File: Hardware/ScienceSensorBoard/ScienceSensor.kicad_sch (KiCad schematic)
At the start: 93 parts, among them J1 Conn_02x03_Counter_Clockwise, J2 RJ45_LED_Shielded, Q1 SI4156DY, Q10 BSS138, Q11 SI4156DY, Q2 SI4156DY, Q3 SI4156DY, Q4 BSS138, Q5 BSS138, Q6 BSS138, Q7 BSS138, Q8 BSS138, Q9 BSS138, U1 TSR_1-2450, U2 OKI-78SR-3.3_1.5-W36H-C, U3 Teensy4.1_DEV-16771, U6 IRS2005S, U7 IRS2005S

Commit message: Labels
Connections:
- net +12V: now also Conn6.1; no longer Conn6.2
- net GND: now also Conn6.2; no longer Conn6.3
- net Micro_ENC: now also Conn6.3; no longer Conn6.1
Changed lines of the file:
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@@
     (stroke (width 0) (type default) (color 0 0 0 0))
   )
-  (wire (pts (xy 123.825 72.39) (xy 123.825 78.105))
+  (wire (pts (xy 130.175 64.77) (xy 124.46 64.77))
     (stroke (width 0) (type default) (color 0 0 0 0))
   )
@@
     (stroke (width 0) (type default) (color 0 0 0 0))
   )
-  (wire (pts (xy 132.715 72.39) (xy 133.985 72.39))
+  (wire (pts (xy 127.635 71.12) (xy 127.635 73.025))
     (stroke (width 0) (type default) (color 0 0 0 0))
   )
@@
     (stroke (width 0) (type default) (color 0 0 0 0))
   )
-  (wire (pts (xy 127.635 72.39) (xy 127.635 73.025))
+  (wire (pts (xy 124.46 64.77) (xy 124.46 65.405))
     (stroke (width 0) (type default) (color 0 0 0 0))
   )
@@
     (stroke (width 0) (type default) (color 0 0 0 0))
   )
-  (wire (pts (xy 123.825 72.39) (xy 127.635 72.39))
+  (wire (pts (xy 130.175 64.77) (xy 130.175 73.025))
     (stroke (width 0) (type default) (color 0 0 0 0))
   )
@@
     (stroke (width 0) (type default) (color 0 0 0 0))
   )
-  (wire (pts (xy 130.175 71.12) (xy 130.175 73.025))
-    (stroke (width 0) (type default) (color 0 0 0 0))
-  )
   (wire (pts (xy 180.34 109.22) (xy 180.34 110.49))
     (stroke (width 0) (type default) (color 0 0 0 0))
@@
   )
   (wire (pts (xy 162.56 101.6) (xy 162.56 95.25))
+    (stroke (width 0) (type default) (color 0 0 0 0))
+  )
+  (wire (pts (xy 126.365 71.12) (xy 127.635 71.12))
     (stroke (width 0) (type default) (color 0 0 0 0))
   )
@@
     )
   )
-  (global_label "Micro_ENC" (shape output) (at 133.985 72.39 0) (fields_autoplaced)
-    (effects (font (size 1.27 1.27)) (justify left))
-    (property "Intersheet References" "${INTERSHEET_REFS}" (id 0) (at 146.1063 72.3106 0)
-      (effects (font (size 1.27 1.27)) (justify left) hide)
+  (global_label "Micro_ENC" (shape output) (at 126.365 71.12 180) (fields_autoplaced)
+    (effects (font (size 1.27 1.27)) (justify right))
+    (property "Intersheet References" "${INTERSHEET_REFS}" (id 0) (at 114.2437 71.1994 0)
+      (effects (font (size 1.27 1.27)) (justify right) hide)
     )
   )
@@
     (pin "2")
   )
-  (symbol (lib_id "power:+12V") (at 130.175 71.12 0) (unit 1)
-    (in_bom yes) (on_board yes) (fields_autoplaced)
-    (property "Reference" "#PWR0101" (id 0) (at 130.175 74.93 0)
-      (effects (font (size 1.27 1.27)) hide)
-    )
-    (property "Value" "+12V" (id 1) (at 130.175 67.5442 0))
-    (property "Footprint" "" (id 2) (at 130.175 71.12 0)
-      (effects (font (size 1.27 1.27)) hide)
-    )
-    (property "Datasheet" "" (id 3) (at 130.175 71.12 0)
+  (symbol (lib_id "power:+12V") (at 132.715 72.39 0) (unit 1)
+    (in_bom yes) (on_board yes) (fields_autoplaced)
+    (property "Reference" "#PWR0101" (id 0) (at 132.715 76.2 0)
+      (effects (font (size 1.27 1.27)) hide)
+    )
+    (property "Value" "+12V" (id 1) (at 132.715 68.8142 0))
+    (property "Footprint" "" (id 2) (at 132.715 72.39 0)
+      (effects (font (size 1.27 1.27)) hide)
+    )
+    (property "Datasheet" "" (id 3) (at 132.715 72.39 0)
       (effects (font (size 1.27 1.27)) hide)
     )
@@
     (pin "3")
   )
-  (symbol (lib_id "power:GND") (at 123.825 78.105 0) (unit 1)
-    (in_bom yes) (on_board yes)
-    (property "Reference" "#PWR014" (id 0) (at 123.825 84.455 0)
-      (effects (font (size 1.27 1.27)) hide)
-    )
-    (property "Value" "GND" (id 1) (at 120.65 80.01 0))
-    (property "Footprint" "" (id 2) (at 123.825 78.105 0)
-      (effects (font (size 1.27 1.27)) hide)
-    )
-    (property "Datasheet" "" (id 3) (at 123.825 78.105 0)
-      (effects (font (size 1.27 1.27)) hide)
-    )
+  (symbol (lib_id "power:GND") (at 124.46 65.405 0) (unit 1)
+    (in_bom yes) (on_board yes)
+    (property "Reference" "#PWR014" (id 0) (at 124.46 71.755 0)
+      (effects (font (size 1.27 1.27)) hide)
+    )
+    (property "Value" "GND" (id 1) (at 121.285 67.31 0))
+    (property "Footprint" "" (id 2) (at 124.46 65.405 0)
+      (effects (font (size 1.27 1.27)) hide)
+    )
+    (property "Datasheet" "" (id 3) (at 124.46 65.405 0)
+      (effects (font (size 1.27 1.27)) hide)
+    )

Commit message: Molex_SL_06
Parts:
- removed Conn4: Molex_SL_07, MRDT_Connectors:MOLEX_SL_07_Horizontal, symbol MRDT_Connectors:Molex_SL_07
- added Conn4: Molex_SL_06, UVLEDs:705550040, symbol Molex_SL_06:Molex_SL_06
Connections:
- net +12V: now also Conn4.1
- net GND: now also Conn4.2
- net LED_275: now also Conn4.4
- net LED_280: now also Conn4.5
- net LED_315: now also Conn4.6
- no-connect marks 39 -> 38
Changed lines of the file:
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@@
   (no_connect (at 78.105 267.97))
   (no_connect (at 37.465 227.33))
-  (no_connect (at 297.18 24.765))
   (no_connect (at 37.465 234.95))
   (no_connect (at 78.105 199.39))
@@
     (stroke (width 0) (type default) (color 0 0 0 0))
   )
-  (wire (pts (xy 292.1 34.925) (xy 292.1 38.1))
+  (wire (pts (xy 292.1 32.385) (xy 292.1 38.1))
     (stroke (width 0) (type default) (color 0 0 0 0))
   )
@@
     (stroke (width 0) (type default) (color 0 0 0 0))
   )
-  (wire (pts (xy 297.18 34.925) (xy 292.1 34.925))
+  (wire (pts (xy 297.18 32.385) (xy 292.1 32.385))
     (stroke (width 0) (type default) (color 0 0 0 0))
   )
@@
     (stroke (width 0) (type default) (color 0 0 0 0))
   )
-  (wire (pts (xy 281.305 35.56) (xy 281.305 32.385))
+  (wire (pts (xy 281.305 29.845) (xy 281.305 35.56))
     (stroke (width 0) (type default) (color 0 0 0 0))
   )
@@
     (stroke (width 0) (type default) (color 0 0 0 0))
   )
-  (wire (pts (xy 259.715 27.305) (xy 297.18 27.305))
+  (wire (pts (xy 259.715 24.765) (xy 297.18 24.765))
     (stroke (width 0) (type default) (color 0 0 0 0))
   )
@@
     (stroke (width 0) (type default) (color 0 0 0 0))
   )
-  (wire (pts (xy 270.51 33.02) (xy 270.51 29.845))
+  (wire (pts (xy 270.51 27.305) (xy 270.51 33.02))
     (stroke (width 0) (type default) (color 0 0 0 0))
   )
@@
     (stroke (width 0) (type default) (color 0 0 0 0))
   )
-  (wire (pts (xy 270.51 29.845) (xy 297.18 29.845))
+  (wire (pts (xy 270.51 27.305) (xy 297.18 27.305))
     (stroke (width 0) (type default) (color 0 0 0 0))
   )
@@
     (stroke (width 0) (type default) (color 0 0 0 0))
   )
-  (wire (pts (xy 281.305 32.385) (xy 297.18 32.385))
+  (wire (pts (xy 281.305 29.845) (xy 297.18 29.845))
     (stroke (width 0) (type default) (color 0 0 0 0))
   )
@@
     (pin "3")
   )
-  (symbol (lib_id "MRDT_Connectors:Molex_SL_07") (at 302.26 36.195 0) (unit 1)
-    (in_bom yes) (on_board yes)
-    (property "Reference" "Conn4" (id 0) (at 301.625 38.2816 0)
-      (effects (font (size 1.524 1.524)) (justify left))
-    )
-    (property "Value" "Molex_SL_07" (id 1) (at 301.625 41.275 0)
-      (effects (font (size 1.524 1.524)) (justify left))
-    )
-    (property "Footprint" "MRDT_Connectors:MOLEX_SL_07_Horizontal" (id 2) (at 302.26 31.115 0)
-      (effects (font (size 1.524 1.524)) hide)
-    )
-    (property "Datasheet" "" (id 3) (at 302.26 31.115 0)
-      (effects (font (size 1.524 1.524)) hide)
-    )
-    (pin "1")
-    (pin "2")
-    (pin "3")
-    (pin "4")
-    (pin "5")
-    (pin "6")
-    (pin "7")
-  )
   (symbol (lib_id "power:+5V") (at 137.16 20.32 0) (unit 1)
     (in_bom yes) (on_board yes) (fields_autoplaced)
@@
     (pin "1")
   )
+  (symbol (lib_id "Molex_SL_06:Molex_SL_06") (at 302.26 31.115 0) (unit 1)
+    (in_bom yes) (on_board yes) (fields_autoplaced)
+    (property "Reference" "Conn4" (id 0) (at 305.435 25.0588 0)
+      (effects (font (size 1.524 1.524)) (justify left))
+    )
+    (property "Value" "Molex_SL_06" (id 1) (at 305.435 28.0522 0)
+      (effects (font (size 1.524 1.524)) (justify left))
+    )
+    (property "Footprint" "UVLEDs:705550040" (id 2) (at 302.26 31.115 0)
+      (effects (font (size 1.524 1.524)) hide)
+    )
+    (property "Datasheet" "" (id 3) (at 302.26 31.115 0)
+      (effects (font (size 1.524 1.524)) hide)
+    )
+    (pin "1")
+    (pin "2")
+    (pin "3")
+    (pin "4")
+    (pin "5")
+    (pin "6")
+  )
   (symbol (lib_id "power:GND") (at 294.005 57.15 90) (unit 1)
     (in_bom yes) (on_board yes)
@@
       (reference "Conn3") (unit 1) (value "Molex_SL_02") (footprint "MRDT_Connectors:MOLEX_SL_02_Horizontal")
     )
-    (path "/2cca1221-a56d-46b9-abdb-f313a2558695"
-      (reference "Conn4") (unit 1) (value "Molex_SL_07") (footprint "MRDT_Connectors:MOLEX_SL_07_Horizontal")
+    (path "/e8ba4c58-43c8-4e60-828b-fab781a9437e"
+      (reference "Conn4") (unit 1) (value "Molex_SL_06") (footprint "UVLEDs:705550040")
     )
     (path "/726f2370-5511-4905-9eb4-028092273805"

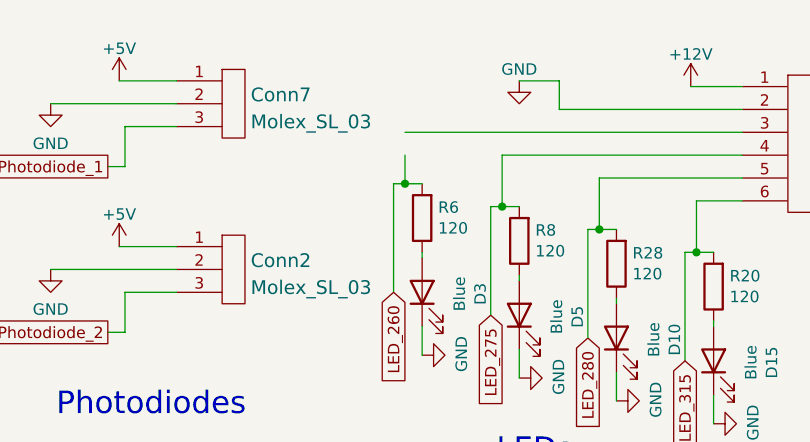
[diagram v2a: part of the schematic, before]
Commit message: Fixed Schematic error, Labeled some LEDs
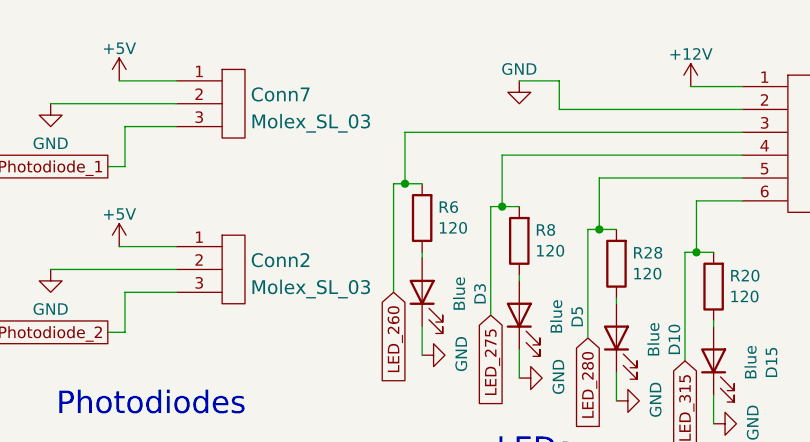
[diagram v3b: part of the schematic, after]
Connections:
- net LED_260: now also Conn4.3
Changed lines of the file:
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@@
-    (stroke (width 0) (type default) (color 0 0 0 0))
-  )
-  (wire (pts (xy 259.715 30.48) (xy 259.715 27.305))
     (stroke (width 0) (type default) (color 0 0 0 0))
   )
@@
     (stroke (width 0) (type default) (color 0 0 0 0))
   )
+  (wire (pts (xy 259.715 24.765) (xy 259.715 30.48))
+    (stroke (width 0) (type default) (color 0 0 0 0))
+  )

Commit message: Replaced HBridge & Encoder w/ servo
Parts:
- removed C10, C8: 0.1u, Capacitor_SMD:C_0603_1608Metric_Pad1.08x0.95mm_HandSolder, symbol Device:C
- removed C9: 10u, Capacitor_SMD:C_0603_1608Metric_Pad1.08x0.95mm_HandSolder, symbol Device:C_Small
- removed Conn5: AndersonPP, MRDT_Connectors:Square_Anderson_2_H_Side_By_Side, symbol MRDT_Connectors:AndersonPP
- removed Conn6: Molex_SL_03, MRDT_Connectors:MOLEX_SL_03_Horizontal, symbol MRDT_Connectors:Molex_SL_03
- removed D11, D14: D_Small, Diode_SMD:D_0603_1608Metric_Pad1.05x0.95mm_HandSolder, symbol Device:D_Small
- removed D12, D13: Pink, LED_SMD:LED_0603_1608Metric_Pad1.05x0.95mm_HandSolder, symbol Device:LED_Small
- removed Q1, Q11, Q2, Q3: SI4156DY, Package_SO:SOIC-8_3.9x4.9mm_P1.27mm, symbol Transistor_FET:FDS2734
- removed R29, R30, R33, R34: 100, Resistor_SMD:R_0603_1608Metric_Pad0.98x0.95mm_HandSolder, symbol Device:R
- removed R31, R32: 120, Resistor_SMD:R_0603_1608Metric_Pad0.98x0.95mm_HandSolder, symbol Device:R
- removed U6, U7: IRS2005S, Package_SO:SOIC-8_3.9x4.9mm_P1.27mm, symbol Driver_FET:IRS2005S
- added Conn?: Molex_SL_03, MRDT_Connectors:MOLEX_SL_03_Horizontal, symbol MRDT_Connectors:Molex_SL_03
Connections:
- net +5V: now also Conn?.1
- net GND: now also Conn?.2
- net Micro_Servo2: now reaches U3.38 (A14)
- net Micro_Servo2: now also Conn?.3
- net Micro_ENC: no longer names the net of U3.21 (A7)
- net Micro_FWD: no longer names the net of U3.14 (A0)
- net Micro_RVS: no longer names the net of U3.15 (A1)
- net Micro_Servo renamed Micro_Servo1
- no-connect marks 38 -> 40
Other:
- note added: "To be updated with new detector"
- note removed: "Encoder"
- note removed: "H-Bridge"
- moved on the sheet: Conn2, Conn3, Conn4, Conn7, D10, D15, D3, D4, D5, R20, R28, R6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

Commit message: CCD, LED changes
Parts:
- removed Conn2, Conn7: Molex_SL_03, MRDT_Connectors:MOLEX_SL_03_Horizontal, symbol MRDT_Connectors:Molex_SL_03
- added Conn?: Molex_SL_06, UVLEDs:705550040, symbol Molex_SL_06:Molex_SL_06
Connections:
- net +3V3: now also Conn?.1
- net GND: now also Conn?.2
- net CCD_ICG: now reaches U3.39 (A15)
- net CCD_ICG: now also Conn?.5
- net CCD_SH: now reaches U3.40 (A16)
- net CCD_SH: now also Conn?.4
- net Photodiode_1 renamed CCD_MC
- net CCD_MC: now also Conn?.3
- net Photodiode_2 renamed CCD_OS
- net CCD_OS: now also Conn?.6
- no-connect marks 40 -> 37
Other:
- note added: "LEDs & Detector"
- note added: "TCD1304AP CCD"
- note removed: "LEDs & Photodiode"
- note removed: "Photodiodes"
- note removed: "To be updated with new detector"

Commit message: Layout updated for LEDs and Science Sensor Board, schematic for CCD
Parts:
- gave numbers to parts that had none: 2
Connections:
- net Micro_Servo2: now also U3.23 (A9); no longer U3.38 (A14)
- no-connect marks 37 -> 38
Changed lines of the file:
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@@
   )
   (no_connect (at 37.465 240.03))
+  (no_connect (at 78.105 255.27))
   (no_connect (at 78.105 229.87))
   (no_connect (at 94.615 168.91))
@@
     (stroke (width 0) (type default) (color 0 0 0 0))
   )
-  (wire (pts (xy 78.105 255.27) (xy 83.185 255.27))
+  (wire (pts (xy 78.105 267.97) (xy 83.185 267.97))
     (stroke (width 0) (type default) (color 0 0 0 0))
   )
@@
     )
   )
-  (global_label "Micro_Servo2" (shape output) (at 83.185 255.27 0) (fields_autoplaced)
+  (global_label "Micro_Servo2" (shape output) (at 83.185 267.97 0) (fields_autoplaced)
     (effects (font (size 1 1)) (justify left))
-    (property "Intersheet References" "${INTERSHEET_REFS}" (id 0) (at 94.8245 255.2075 0)
+    (property "Intersheet References" "${INTERSHEET_REFS}" (id 0) (at 94.8245 267.9075 0)
       (effects (font (size 1 1)) (justify left) hide)
     )
@@
   (symbol (lib_id "MRDT_Connectors:Molex_SL_03") (at 147.955 47.625 0) (unit 1)
     (in_bom yes) (on_board yes) (fields_autoplaced)
-    (property "Reference" "Conn?" (id 0) (at 151.13 42.8388 0)
+    (property "Reference" "Conn2" (id 0) (at 151.13 42.8388 0)
       (effects (font (size 1.524 1.524)) (justify left))
     )
@@
   (symbol (lib_id "Molex_SL_06:Molex_SL_06") (at 271.78 99.695 0) (unit 1)
     (in_bom yes) (on_board yes) (fields_autoplaced)
-    (property "Reference" "Conn?" (id 0) (at 274.955 93.6388 0)
+    (property "Reference" "Conn5" (id 0) (at 274.955 93.6388 0)
       (effects (font (size 1.524 1.524)) (justify left))
     )
@@
   (symbol (lib_id "power:+3V3") (at 260.35 88.265 0) (unit 1)
     (in_bom yes) (on_board yes) (fields_autoplaced)
-    (property "Reference" "#PWR?" (id 0) (at 260.35 92.075 0)
+    (property "Reference" "#PWR037" (id 0) (at 260.35 92.075 0)
       (effects (font (size 1.27 1.27)) hide)
     )
@@
   (symbol (lib_id "power:+5V") (at 136.525 41.275 0) (unit 1)
     (in_bom yes) (on_board yes) (fields_autoplaced)
-    (property "Reference" "#PWR?" (id 0) (at 136.525 45.085 0)
+    (property "Reference" "#PWR022" (id 0) (at 136.525 45.085 0)
       (effects (font (size 1.27 1.27)) hide)
     )
@@
   (symbol (lib_id "power:GND") (at 125.095 43.815 0) (unit 1)
     (in_bom yes) (on_board yes) (fields_autoplaced)
-    (property "Reference" "#PWR?" (id 0) (at 125.095 50.165 0)
+    (property "Reference" "#PWR014" (id 0) (at 125.095 50.165 0)
       (effects (font (size 1.27 1.27)) hide)
     )
@@
       (reference "#PWR013") (unit 1) (value "GND") (footprint "")
     )
+    (path "/f84a6be2-e53a-41ef-8d50-c4ba4a360cf2"
+      (reference "#PWR014") (unit 1) (value "GND") (footprint "")
+    )
     (path "/a3a1a4c2-7b43-4b66-b2fa-00336742ef9e"
       (reference "#PWR015") (unit 1) (value "GND") (footprint "")
@@
       (reference "#PWR021") (unit 1) (value "+3V3") (footprint "")
     )
+    (path "/a03c9a29-5797-44f0-99be-b60513c119e6"
+      (reference "#PWR022") (unit 1) (value "+5V") (footprint "")
+    )
     (path "/f13257ce-1afa-4210-ae15-48a4a0e8767c"
       (reference "#PWR023") (unit 1) (value "+5V") (footprint "")
@@
       (reference "#PWR036") (unit 1) (value "+3V3") (footprint "")
     )
+    (path "/7307226a-1726-450c-b33f-9ca1bcfb5b4e"
+      (reference "#PWR037") (unit 1) (value "+3V3") (footprint "")
+    )
     (path "/1e719a26-9494-4397-9f3e-0963257a6af1"
       (reference "#PWR040") (unit 1) (value "+5V") (footprint "")
@@
       (reference "#PWR0108") (unit 1) (value "+5V") (footprint "")
     )
-    (path "/7307226a-1726-450c-b33f-9ca1bcfb5b4e"
-      (reference "#PWR?") (unit 1) (value "+3V3") (footprint "")
-    )
-    (path "/a03c9a29-5797-44f0-99be-b60513c119e6"
-      (reference "#PWR?") (unit 1) (value "+5V") (footprint "")
-    )
-    (path "/f84a6be2-e53a-41ef-8d50-c4ba4a360cf2"
-      (reference "#PWR?") (unit 1) (value "GND") (footprint "")
-    )
     (path "/7becaed6-99a4-49f3-99dd-3fce229dac4a"
       (reference "C1") (unit 1) (value "0.1uF") (footprint "Capacitor_SMD:C_0603_1608Metric_Pad1.08x0.95mm_HandSolder")
@@
       (reference "Conn1") (unit 2) (value "AndersonPP") (footprint "MRDT_Connectors:Square_Anderson_2_H_Side_By_Side")
     )
+    (path "/35f3c6b6-46ab-4b07-9dc5-fca0ff70b9e9"
+      (reference "Conn2") (unit 1) (value "Molex_SL_03") (footprint "MRDT_Connectors:MOLEX_SL_03_Horizontal")
+    )
     (path "/362043ba-7077-4355-842f-ed4e21c764a7"
       (reference "Conn3") (unit 1) (value "Molex_SL_02") (footprint "MRDT_Connectors:MOLEX_SL_02_Horizontal")
@@
       (reference "Conn4") (unit 1) (value "Molex_SL_06") (footprint "UVLEDs:705550040")
     )
+    (path "/6b5caef2-e1fb-43d2-90ee-f19eab3f6b8f"
+      (reference "Conn5") (unit 1) (value "Molex_SL_06") (footprint "UVLEDs:705550040")
+    )
     (path "/6a2e2e5d-609f-433a-995e-8e1ddb8bf56f"
       (reference "Conn8") (unit 1) (value "Molex_SL_04") (footprint "MRDT_Connectors:MOLEX_SL_04_Horizontal")
@@
       (reference "Conn13") (unit 1) (value "Molex_SL_04") (footprint "MRDT_Connectors:MOLEX_SL_04_Horizontal")
     )
-    (path "/35f3c6b6-46ab-4b07-9dc5-fca0ff70b9e9"
-      (reference "Conn?") (unit 1) (value "Molex_SL_03") (footprint "MRDT_Connectors:MOLEX_SL_03_Horizontal")
-    )
-    (path "/6b5caef2-e1fb-43d2-90ee-f19eab3f6b8f"
-      (reference "Conn?") (unit 1) (value "Molex_SL_06") (footprint "UVLEDs:705550040")
-    )
     (path "/00000000-0000-0000-0000-000063231caf"

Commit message: Started cleaning up layout
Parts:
- Conn4, Conn5: footprint UVLEDs:705550040 -> Connector_Molex:Molex_SL_171971-0006_1x06_P2.54mm_Vertical
- Q10, Q4, Q5, Q6, Q7, Q8, Q9: footprint Package_TO_SOT_SMD:SOT-323_SC-70_Handsoldering -> Package_TO_SOT_SMD:SOT-23
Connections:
- net +5V: now also U3.VIN
- net GND: now also J2.SH
- no-connect marks 38 -> 36
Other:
- moved on the sheet: D1, R1

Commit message: Finished traces
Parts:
- removed C2: 10 uF, Capacitor_SMD:C_0603_1608Metric_Pad1.08x0.95mm_HandSolder, symbol Device:C_Polarized_US
- removed C4: 10uF, Capacitor_SMD:C_0603_1608Metric_Pad1.08x0.95mm_HandSolder, symbol Device:C
- removed U2: OKI-78SR-3.3_1.5-W36H-C, MRDT_Devices:OKI_Horizontal, symbol Converter_DCDC:OKI-78SR-3.3_1.5-W36H-C
- renumbered Conn9 to Conn10, Conn10 to Conn11, Conn3 to Conn2, Conn2 to Conn3, Conn12 to Conn4, Conn4 to Conn6, Conn11 to Conn7, Conn13 to Conn8, Conn8 to Conn9, D6 to D10, D7 to D11, D8 to D12, D9 to D13, D4 to D3, D3 to D4, D10 to D6, D15 to D7, D16 to D8, D17 to D9, J2 to J1, J1 to J2, Q4 to Q1, Q5 to Q2, Q6 to Q3, Q7 to Q4, Q8 to Q5, Q9 to Q6, Q10 to Q7, R11 to R10, R13 to R11, R6 to R12, R14 to R13, R15 to R14, R16 to R15, R8 to R16, R28 to R17, R17 to R18, R18 to R19, R19 to R20, R20 to R21, R27 to R22, R21 to R23, R26 to R24, R22 to R25, R23 to R26, R24 to R27, R25 to R28, R35 to R29, R7 to R3, R3 to R4, R4 to R5, R5 to R6, R12 to R7, R9 to R8, R10 to R9, U3 to U2
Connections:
- net CCD_ICG: now also U2.40 (A16); no longer U2.39 (A15)
- net CCD_MC: now also U2.16 (A2); no longer U2.24 (A10)
- net CCD_OS: now also U2.17 (A3); no longer U2.25 (A11)
- net CCD_SH: now also U2.39 (A15); no longer U2.40 (A16)
- net CH4_RX: now also U2.14 (A0); no longer U2.1 (TX1)
- net CH4_TX: now also U2.15 (A1); no longer U2.0 (RX1)
- net GND: now also U2.USB_GND1 (USB_GND), U2.USB_GND2 (USB_GND)
- net LED_260: now also U2.18 (A4); no longer U2.19 (A5)
- net LED_275: now also U2.19 (A5); no longer U2.18 (A4)
- net LED_280: now also U2.20 (A6); no longer U2.17 (A3)
- net LED_315: now also U2.21 (A7); no longer U2.16 (A2)
- net Micro_Servo1: now also U2.25 (A11); no longer U2.26 (A12)
- net Micro_Servo2: now also U2.24 (A10); no longer U2.23 (A9)
- net Teensy_CO2_RX: now also U2.0 (RX1); no longer U2.28 (RX7)
- net Teensy_CO2_TX: now also U2.1 (TX1); no longer U2.29 (TX7)
- no-connect marks 36 -> 35
